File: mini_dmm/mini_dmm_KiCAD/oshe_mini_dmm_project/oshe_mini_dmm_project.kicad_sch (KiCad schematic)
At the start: 41 parts, among them J1 FTDI Basic, J2 DISPLAY, J3 TEST LEAD CONNECTIONS, SW1 MODE SELECT, SW2 PTS526 SK15 SMTR2 LFS, SW3 SW_DPDT_x2, U1 LM324, U2 BU91796FS-ME2, U3 ATmega328P-A, U4 LM2664M6, Y1 16MHz

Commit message: Made PCB updates
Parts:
- added C1, C2: 1uF, Capacitor_SMD:C_0805_2012Metric_Pad1.18x1.45mm_HandSolder, symbol Device:C
- J1: renamed from J2; footprint (none) -> Mini_DMM_Footprint_Library:LCD-S401M16KR-81359
- J2: renamed from J3; footprint (none) -> Connector_PinHeader_2.54mm:PinHeader_1x06_P2.54mm_Horizontal
- SW1: footprint (none) -> Mini_DMM_Footprint_Library:SMT_FS
- SW2: footprint DMM_Footprint_Library:SMT_FS -> Mini_DMM_Footprint_Library:SMT_FS
- SW3: footprint (none) -> Mini_DMM_Footprint_Library:SW_JS102011SAQN
- renumbered C8 to C10, C1 to C3, C2 to C4, C3 to C5, C4 to C6, C5 to C7, C6 to C8, C7 to C9, F3 to F2, F2 to F3, J1 to J3, R16 to R10, R17 to R11, R14 to R12, R15 to R13, R10 to R6, R11 to R7, R12 to R8, R13 to R9
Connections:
- net +3.3V: now also C1.2
- net -3.3V: now also C2.1
- net A4/SDA: now also U2.30 (SDA)
- net A5/SCL: now also U2.29 (SCL)
- net GND: now also U2.26 (TEST_1), U2.27 (TEST_2), U2.28 (OSCIN), C1.1, C2.2
- net LEAD_2: now also J2.4 (Pin_4); no longer J2.2 (Pin_2)
- net LEAD_4: now also J2.2 (Pin_2); no longer J2.4 (Pin_4)
- no-connect marks 16 -> 15
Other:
- moved on the sheet: D1, D2, D3, D4, R6, R7, R8, R9, SW1, U1E

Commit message: PCB Updated
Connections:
- net Clock-: now reaches C10.2, U3.8 (XTAL2/PB7), Y1.1
- net Clock+: now reaches C9.1, U3.7 (XTAL1/PB6), Y1.2

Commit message: Finished PCB
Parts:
- removed J2: TEST LEAD CONNECTIONS, Connector_PinHeader_2.54mm:PinHeader_1x06_P2.54mm_Horizontal, symbol Connector_Generic:Conn_01x06
- removed R10: 300, Resistor_SMD:R_0805_2012Metric_Pad1.20x1.40mm_HandSolder, symbol Device:R_US
- removed R11: 1k, Resistor_SMD:R_0805_2012Metric_Pad1.20x1.40mm_HandSolder, symbol Device:R_US
- removed SW1: MODE SELECT, Mini_DMM_Footprint_Library:SMT_FS, symbol Switch:SW_Push
- added J2: ICSP, Connector_PinHeader_2.54mm:PinHeader_2x03_P2.54mm_Horizontal, symbol Connector_Generic:Conn_02x03_Top_Bottom
- added J4: TEST LEAD CONNECTIONS, Connector_PinHeader_2.54mm:PinHeader_1x04_P2.54mm_Horizontal, symbol Connector_Generic:Conn_01x04
- added SW1: PTS526 SK15 SMTR2 LFS, Mini_DMM_Footprint_Library:SMT_FS, symbol Mini_DMM_Library:PTS526_SK15_SMTR2_LFS
- C10: renamed from C7; value 1uF -> 10uF
- C8: renamed from C4; value 1uF -> 10uF
- C9: renamed from C6; value 1uF -> 10uF
- J1: renamed from J3; footprint Connector_PinSocket_2.54mm:PinSocket_1x06_P2.54mm_Vertical -> Connector_PinHeader_2.54mm:PinHeader_1x06_P2.54mm_Horizontal; now fitted
- renumbered C3 to C1, C5 to C2, C8 to C3, C9 to C4, C10 to C5, C1 to C6, C2 to C7, J1 to J3, R12 to R10, R13 to R11, U3 to U2, U2 to U3
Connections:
- net +3.3V: now also J2.5 (Pin_5)
- net A2: now also U1.13 (-), U1.14; no longer U1.8, U1.9 (-)
- net A3: now also U1.8, U1.9 (-); no longer U1.13 (-), U1.14
- net D2: no longer D1.2 (A)
- net D3: no longer D2.2 (A)
- net D4: no longer D3.2 (A)
- net D5: now also D3.2 (A); no longer D4.2 (A)
- net D6: now also D2.2 (A)
- net D7: now also D1.2 (A)
- net D8: now also SW1.1, SW1.2
- net D9: now also D4.2 (A)
- net GND: now also U3.23 (VLCD), J2.6 (Pin_6), SW1.3, SW1.4
- net LEAD_1: now also J4.1 (Pin_1)
- net LEAD_2: now also J4.4 (Pin_4)
- net LEAD_3: now also J4.3 (Pin_3)
- net LEAD_4: now also J4.2 (Pin_2)
- net MISO/D12: now also J2.1 (Pin_1)
- net MOSI/D11: now also J2.2 (Pin_2)
- net SCK/D13: now also J2.3 (Pin_3)
- net RESET: now reaches C3.1, R11.1, SW2.1, SW2.2, U2.29 (~{RESET}/PC6)
- net RESET: now also J2.4 (Pin_4)
- no-connect marks 15 -> 13
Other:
- note removed: "Add in pins to flash IC"
- note removed: "VLCD wants 2.45 V or higher Voltage Divider to create 2.53 V"
- moved on the sheet: C1, C2, C3, C4, C5, D1, D2, D3, D4, D5, R10, R11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

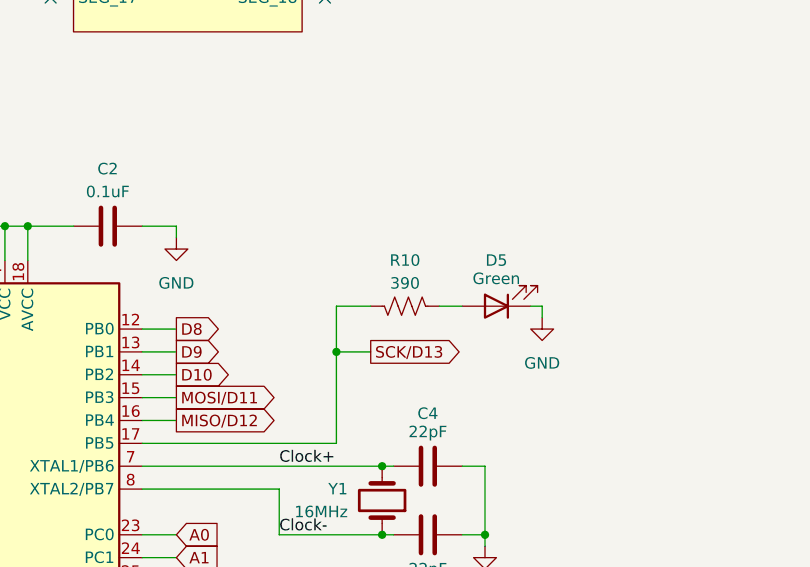
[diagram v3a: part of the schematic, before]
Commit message: updated led resistor
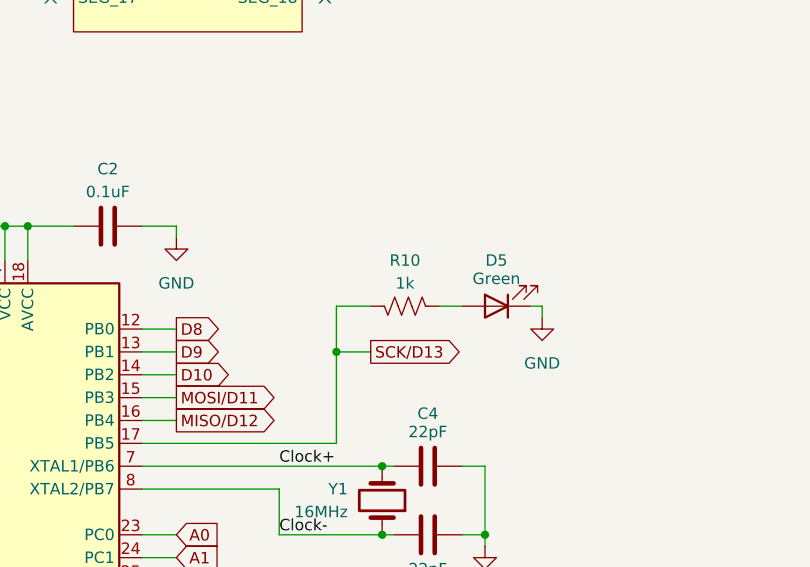
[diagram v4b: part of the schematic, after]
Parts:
- R10: value 390 -> 1k
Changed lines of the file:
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@@
 			)
 		)
-		(property "Value" "390"
+		(property "Value" "1k"
 			(at 246.38 100.33 90)
 			(effects

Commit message: Revert "Merge branch 'main' of https://github.com/peterk-mtu/oshe-dmm"
This reverts commit ce5d962f54be2277657b6d8c67a3a7c391f0a935, reversing
changes made to f95ec51989ec9ec0648d62f0b87f0342297760cd.
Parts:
- R10: value 1k -> 390
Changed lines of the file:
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@@
 			)
 		)
-		(property "Value" "1k"
+		(property "Value" "390"
 			(at 246.38 100.33 90)
 			(effects
